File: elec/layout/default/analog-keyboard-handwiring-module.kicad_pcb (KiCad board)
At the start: 2 copper layers, 95.2 x 95.2 mm, 224 parts

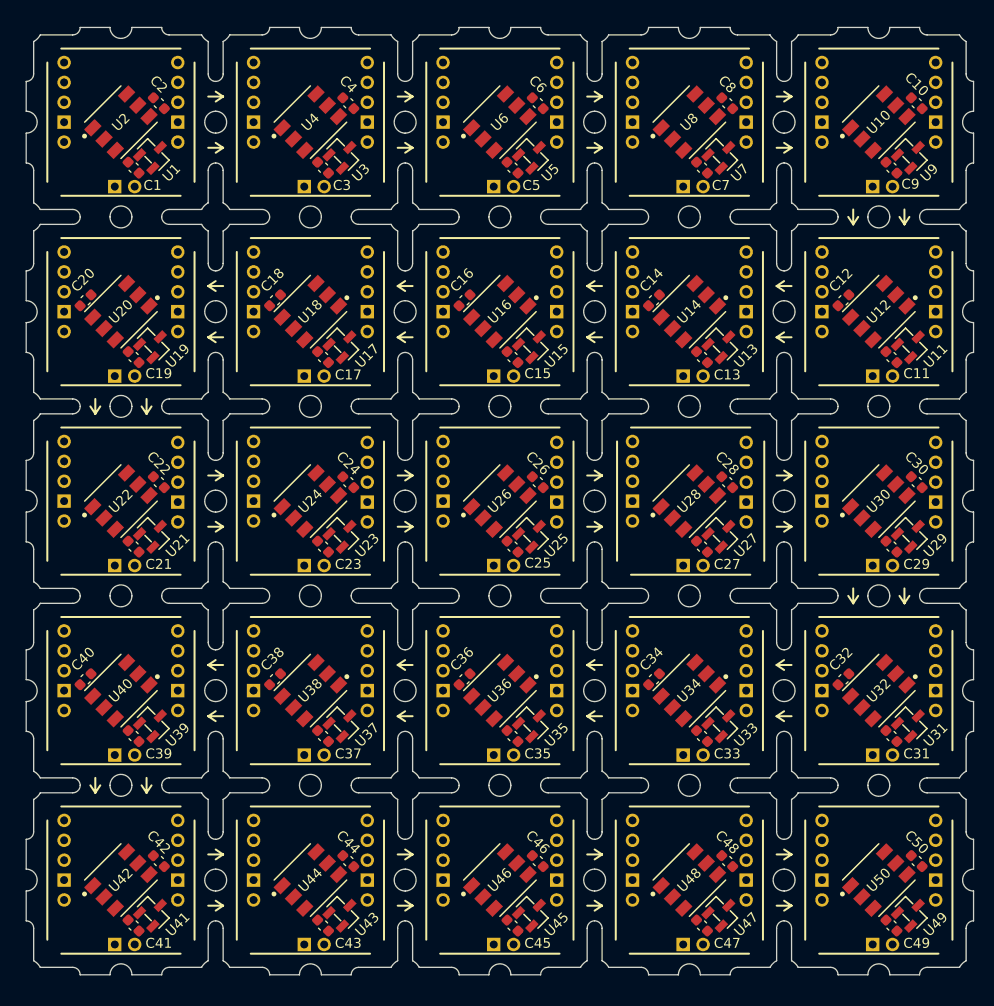
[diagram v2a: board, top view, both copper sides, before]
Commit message: Improve labels and move hall signal connector a little
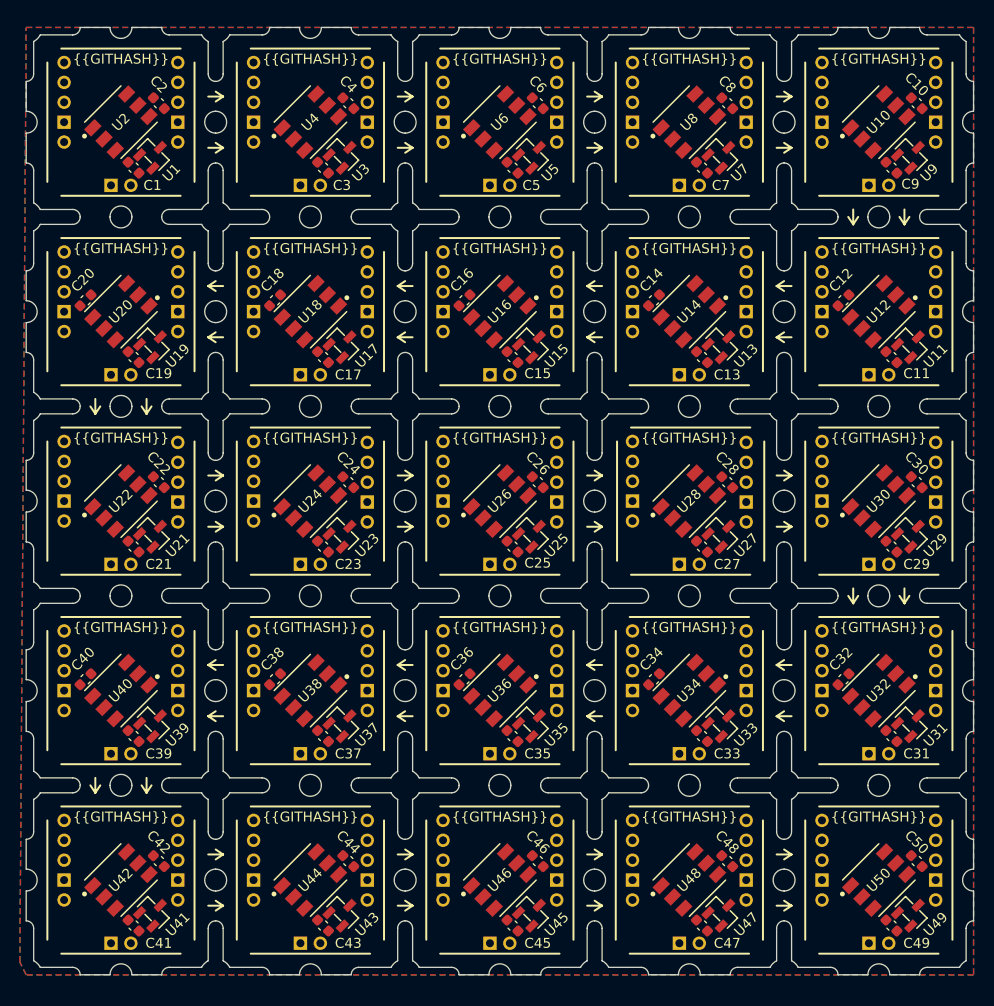
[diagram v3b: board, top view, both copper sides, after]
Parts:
- added kibuzzard-6658D545: G***, kibuzzard-6658D545, B.Cu at (56.3, 129.7)
- added kibuzzard-6658D545: G***, kibuzzard-6658D545, B.Cu at (113.5, 129.7)
- added kibuzzard-6658D545: G***, kibuzzard-6658D545, B.Cu at (113.5, 53.5)
- added kibuzzard-6658D545: G***, kibuzzard-6658D545, B.Cu at (113.5, 91.6)
- added kibuzzard-6658D545: G***, kibuzzard-6658D545, B.Cu at (132.5, 91.6)
- added kibuzzard-6658D545: G***, kibuzzard-6658D545, B.Cu at (75.4, 129.7)
- added kibuzzard-6658D545: G***, kibuzzard-6658D545, B.Cu at (94.4, 53.5)
- added kibuzzard-6658D545: G***, kibuzzard-6658D545, B.Cu at (94.4, 129.7)
- added kibuzzard-6658D545: G***, kibuzzard-6658D545, B.Cu at (56.3, 91.6)
- added kibuzzard-6658D545: G***, kibuzzard-6658D545, B.Cu at (94.4, 91.6)
- added kibuzzard-6658D545: G***, kibuzzard-6658D545, B.Cu at (75.4, 53.5)
- added kibuzzard-6658D545: G***, kibuzzard-6658D545, B.Cu at (56.3, 53.5)
- added kibuzzard-6658D545: G***, kibuzzard-6658D545, B.Cu at (132.5, 53.5)
- added kibuzzard-6658D545: G***, kibuzzard-6658D545, B.Cu at (75.4, 91.6)
- added kibuzzard-6658D545: G***, kibuzzard-6658D545, B.Cu at (132.5, 129.7)
- added kibuzzard-6658D54E: G***, kibuzzard-6658D54E, B.Cu at (75.4, 131.7)
- added kibuzzard-6658D54E: G***, kibuzzard-6658D54E, B.Cu at (56.3, 93.6)
- added kibuzzard-6658D54E: G***, kibuzzard-6658D54E, B.Cu at (113.5, 93.6)
- added kibuzzard-6658D54E: G***, kibuzzard-6658D54E, B.Cu at (56.3, 131.7)
- added kibuzzard-6658D54E: G***, kibuzzard-6658D54E, B.Cu at (94.4, 93.6)
- added kibuzzard-6658D54E: G***, kibuzzard-6658D54E, B.Cu at (132.5, 55.5)
- added kibuzzard-6658D54E: G***, kibuzzard-6658D54E, B.Cu at (94.4, 55.5)
- added kibuzzard-6658D54E: G***, kibuzzard-6658D54E, B.Cu at (113.5, 131.7)
- added kibuzzard-6658D54E: G***, kibuzzard-6658D54E, B.Cu at (56.3, 55.5)
- added kibuzzard-6658D54E: G***, kibuzzard-6658D54E, B.Cu at (75.4, 93.6)
- added kibuzzard-6658D54E: G***, kibuzzard-6658D54E, B.Cu at (132.5, 131.7)
- added kibuzzard-6658D54E: G***, kibuzzard-6658D54E, B.Cu at (113.5, 55.5)
- added kibuzzard-6658D54E: G***, kibuzzard-6658D54E, B.Cu at (132.5, 93.6)
- added kibuzzard-6658D54E: G***, kibuzzard-6658D54E, B.Cu at (94.4, 131.7)
- added kibuzzard-6658D54E: G***, kibuzzard-6658D54E, B.Cu at (75.4, 55.5)
- added kibuzzard-6658D556: G***, kibuzzard-6658D556, B.Cu at (56.8, 133.7)
- added kibuzzard-6658D556: G***, kibuzzard-6658D556, B.Cu at (94.9, 114.7)
- added kibuzzard-6658D556: G***, kibuzzard-6658D556, B.Cu at (56.8, 57.5)
- added kibuzzard-6658D556: G***, kibuzzard-6658D556, B.Cu at (94.9, 76.6)
- added kibuzzard-6658D556: G***, kibuzzard-6658D556, B.Cu at (75.8, 114.7)
- added kibuzzard-6658D556: G***, kibuzzard-6658D556, B.Cu at (133.0, 76.6)
- added kibuzzard-6658D556: G***, kibuzzard-6658D556, B.Cu at (75.8, 57.5)
- added kibuzzard-6658D556: G***, kibuzzard-6658D556, B.Cu at (133.0, 114.7)
- added kibuzzard-6658D556: G***, kibuzzard-6658D556, B.Cu at (133.0, 95.6)
- added kibuzzard-6658D556: G***, kibuzzard-6658D556, B.Cu at (94.9, 57.5)
- added kibuzzard-6658D556: G***, kibuzzard-6658D556, B.Cu at (75.8, 95.6)
- added kibuzzard-6658D556: G***, kibuzzard-6658D556, B.Cu at (56.8, 114.7)
- added kibuzzard-6658D556: G***, kibuzzard-6658D556, B.Cu at (94.9, 133.7)
- added kibuzzard-6658D556: G***, kibuzzard-6658D556, B.Cu at (113.9, 57.5)
- added kibuzzard-6658D556: G***, kibuzzard-6658D556, B.Cu at (113.9, 95.6)
- added kibuzzard-6658D556: G***, kibuzzard-6658D556, B.Cu at (133.0, 57.5)
- added kibuzzard-6658D556: G***, kibuzzard-6658D556, B.Cu at (113.9, 133.7)
- added kibuzzard-6658D556: G***, kibuzzard-6658D556, B.Cu at (56.8, 95.6)
- added kibuzzard-6658D556: G***, kibuzzard-6658D556, B.Cu at (113.9, 76.6)
- added kibuzzard-6658D556: G***, kibuzzard-6658D556, B.Cu at (56.8, 76.6)
- added kibuzzard-6658D556: G***, kibuzzard-6658D556, B.Cu at (75.8, 76.6)
- added kibuzzard-6658D556: G***, kibuzzard-6658D556, B.Cu at (133.0, 133.7)
- added kibuzzard-6658D556: G***, kibuzzard-6658D556, B.Cu at (94.9, 95.6)
- added kibuzzard-6658D556: G***, kibuzzard-6658D556, B.Cu at (113.9, 114.7)
- added kibuzzard-6658D556: G***, kibuzzard-6658D556, B.Cu at (75.8, 133.7)
- added kibuzzard-6658D562: G***, kibuzzard-6658D562, B.Cu at (94.5, 59.5)
- added kibuzzard-6658D562: G***, kibuzzard-6658D562, B.Cu at (94.5, 116.7)
- added kibuzzard-6658D562: G***, kibuzzard-6658D562, B.Cu at (56.4, 59.5)
- added kibuzzard-6658D562: G***, kibuzzard-6658D562, B.Cu at (75.4, 97.6)
- added kibuzzard-6658D562: G***, kibuzzard-6658D562, B.Cu at (75.4, 116.7)
- added kibuzzard-6658D562: G***, kibuzzard-6658D562, B.Cu at (94.5, 135.7)
- added kibuzzard-6658D562: G***, kibuzzard-6658D562, B.Cu at (132.6, 116.7)
- added kibuzzard-6658D562: G***, kibuzzard-6658D562, B.Cu at (94.5, 97.6)
- added kibuzzard-6658D562: G***, kibuzzard-6658D562, B.Cu at (56.4, 116.7)
- added kibuzzard-6658D562: G***, kibuzzard-6658D562, B.Cu at (75.4, 135.7)
- added kibuzzard-6658D562: G***, kibuzzard-6658D562, B.Cu at (113.5, 59.5)
- added kibuzzard-6658D562: G***, kibuzzard-6658D562, B.Cu at (75.4, 78.6)
- added kibuzzard-6658D562: G***, kibuzzard-6658D562, B.Cu at (113.5, 135.7)
- added kibuzzard-6658D562: G***, kibuzzard-6658D562, B.Cu at (113.5, 78.6)
- added kibuzzard-6658D562: G***, kibuzzard-6658D562, B.Cu at (94.5, 78.6)
- added kibuzzard-6658D562: G***, kibuzzard-6658D562, B.Cu at (56.4, 78.6)
- added kibuzzard-6658D562: G***, kibuzzard-6658D562, B.Cu at (113.5, 116.7)
- added kibuzzard-6658D562: G***, kibuzzard-6658D562, B.Cu at (75.4, 59.5)
- added kibuzzard-6658D562: G***, kibuzzard-6658D562, B.Cu at (56.4, 97.6)
- added kibuzzard-6658D562: G***, kibuzzard-6658D562, B.Cu at (132.6, 59.5)
- added kibuzzard-6658D562: G***, kibuzzard-6658D562, B.Cu at (132.6, 78.6)
- added kibuzzard-6658D562: G***, kibuzzard-6658D562, B.Cu at (56.4, 135.7)
- added kibuzzard-6658D562: G***, kibuzzard-6658D562, B.Cu at (132.6, 97.6)
- added kibuzzard-6658D562: G***, kibuzzard-6658D562, B.Cu at (132.6, 135.7)
- added kibuzzard-6658D562: G***, kibuzzard-6658D562, B.Cu at (113.5, 97.6)
- added kibuzzard-6658D56A: G***, kibuzzard-6658D56A, B.Cu at (94.9, 99.6)
- added kibuzzard-6658D56A: G***, kibuzzard-6658D56A, B.Cu at (75.8, 61.5)
- added kibuzzard-6658D56A: G***, kibuzzard-6658D56A, B.Cu at (94.9, 137.7)
- added kibuzzard-6658D56A: G***, kibuzzard-6658D56A, B.Cu at (94.9, 118.7)
- added kibuzzard-6658D56A: G***, kibuzzard-6658D56A, B.Cu at (113.9, 99.6)
- added kibuzzard-6658D56A: G***, kibuzzard-6658D56A, B.Cu at (113.9, 80.6)
- added kibuzzard-6658D56A: G***, kibuzzard-6658D56A, B.Cu at (56.8, 99.6)
- added kibuzzard-6658D56A: G***, kibuzzard-6658D56A, B.Cu at (75.8, 80.6)
- added kibuzzard-6658D56A: G***, kibuzzard-6658D56A, B.Cu at (133.0, 80.6)
- added kibuzzard-6658D56A: G***, kibuzzard-6658D56A, B.Cu at (113.9, 137.7)
- added kibuzzard-6658D56A: G***, kibuzzard-6658D56A, B.Cu at (56.8, 118.7)
- added kibuzzard-6658D56A: G***, kibuzzard-6658D56A, B.Cu at (75.8, 118.7)
- added kibuzzard-6658D56A: G***, kibuzzard-6658D56A, B.Cu at (94.9, 80.6)
- added kibuzzard-6658D56A: G***, kibuzzard-6658D56A, B.Cu at (113.9, 61.5)
- added kibuzzard-6658D56A: G***, kibuzzard-6658D56A, B.Cu at (75.8, 137.7)
- added kibuzzard-6658D56A: G***, kibuzzard-6658D56A, B.Cu at (56.8, 137.7)
- added kibuzzard-6658D56A: G***, kibuzzard-6658D56A, B.Cu at (133.0, 137.7)
- added kibuzzard-6658D56A: G***, kibuzzard-6658D56A, B.Cu at (75.8, 99.6)
- added kibuzzard-6658D56A: G***, kibuzzard-6658D56A, B.Cu at (94.9, 61.5)
- added kibuzzard-6658D56A: G***, kibuzzard-6658D56A, B.Cu at (133.0, 99.6)
- added kibuzzard-6658D56A: G***, kibuzzard-6658D56A, B.Cu at (133.0, 61.5)
- added kibuzzard-6658D56A: G***, kibuzzard-6658D56A, B.Cu at (56.8, 61.5)
- added kibuzzard-6658D56A: G***, kibuzzard-6658D56A, B.Cu at (113.9, 118.7)
- added kibuzzard-6658D56A: G***, kibuzzard-6658D56A, B.Cu at (56.8, 80.6)
- added kibuzzard-6658D56A: G***, kibuzzard-6658D56A, B.Cu at (133.0, 118.7)
- added kibuzzard-6658D6DF: G***, kibuzzard-6658D6DF, B.Cu at (114.9, 64.1)
- added kibuzzard-6658D6DF: G***, kibuzzard-6658D6DF, B.Cu at (57.7, 64.1)
- added kibuzzard-6658D6DF: G***, kibuzzard-6658D6DF, B.Cu at (57.7, 83.1)
- added kibuzzard-6658D6DF: G***, kibuzzard-6658D6DF, B.Cu at (114.9, 140.3)
- added kibuzzard-6658D6DF: G***, kibuzzard-6658D6DF, B.Cu at (133.9, 140.3)
- added kibuzzard-6658D6DF: G***, kibuzzard-6658D6DF, B.Cu at (57.7, 102.2)
- added kibuzzard-6658D6DF: G***, kibuzzard-6658D6DF, B.Cu at (114.9, 121.2)
- added kibuzzard-6658D6DF: G***, kibuzzard-6658D6DF, B.Cu at (76.8, 64.1)
- added kibuzzard-6658D6DF: G***, kibuzzard-6658D6DF, B.Cu at (76.8, 121.2)
- added kibuzzard-6658D6DF: G***, kibuzzard-6658D6DF, B.Cu at (95.8, 64.1)
- added kibuzzard-6658D6DF: G***, kibuzzard-6658D6DF, B.Cu at (114.9, 102.2)
- added kibuzzard-6658D6DF: G***, kibuzzard-6658D6DF, B.Cu at (95.8, 102.2)
- added kibuzzard-6658D6DF: G***, kibuzzard-6658D6DF, B.Cu at (133.9, 102.2)
- added kibuzzard-6658D6DF: G***, kibuzzard-6658D6DF, B.Cu at (95.8, 83.1)
- added kibuzzard-6658D6DF: G***, kibuzzard-6658D6DF, B.Cu at (76.8, 102.2)
- added kibuzzard-6658D6DF: G***, kibuzzard-6658D6DF, B.Cu at (133.9, 121.2)
- added kibuzzard-6658D6DF: G***, kibuzzard-6658D6DF, B.Cu at (76.8, 140.3)
- added kibuzzard-6658D6DF: G***, kibuzzard-6658D6DF, B.Cu at (57.7, 140.3)
- added kibuzzard-6658D6DF: G***, kibuzzard-6658D6DF, B.Cu at (133.9, 64.1)
- added kibuzzard-6658D6DF: G***, kibuzzard-6658D6DF, B.Cu at (95.8, 140.3)
- added kibuzzard-6658D6DF: G***, kibuzzard-6658D6DF, B.Cu at (114.9, 83.1)
- added kibuzzard-6658D6DF: G***, kibuzzard-6658D6DF, B.Cu at (133.9, 83.1)
- added kibuzzard-6658D6DF: G***, kibuzzard-6658D6DF, B.Cu at (76.8, 83.1)
- added kibuzzard-6658D6DF: G***, kibuzzard-6658D6DF, B.Cu at (57.7, 121.2)
- added kibuzzard-6658D6DF: G***, kibuzzard-6658D6DF, B.Cu at (95.8, 121.2)
- added kibuzzard-6658D76C: G***, kibuzzard-6658D76C, B.Cu at (75.0, 104.0)
- added kibuzzard-6658D76C: G***, kibuzzard-6658D76C, B.Cu at (56.0, 142.1)
- added kibuzzard-6658D76C: G***, kibuzzard-6658D76C, B.Cu at (113.1, 142.1)
- added kibuzzard-6658D76C: G***, kibuzzard-6658D76C, B.Cu at (94.1, 65.9)
- added kibuzzard-6658D76C: G***, kibuzzard-6658D76C, B.Cu at (56.0, 65.9)
- added kibuzzard-6658D76C: G***, kibuzzard-6658D76C, B.Cu at (94.1, 123.0)
- added kibuzzard-6658D76C: G***, kibuzzard-6658D76C, B.Cu at (56.0, 123.0)
- added kibuzzard-6658D76C: G***, kibuzzard-6658D76C, B.Cu at (132.2, 104.0)
- added kibuzzard-6658D76C: G***, kibuzzard-6658D76C, B.Cu at (132.2, 142.1)
- added kibuzzard-6658D76C: G***, kibuzzard-6658D76C, B.Cu at (56.0, 104.0)
- added kibuzzard-6658D76C: G***, kibuzzard-6658D76C, B.Cu at (75.0, 65.9)
- added kibuzzard-6658D76C: G***, kibuzzard-6658D76C, B.Cu at (75.0, 142.1)
- added kibuzzard-6658D76C: G***, kibuzzard-6658D76C, B.Cu at (113.1, 104.0)
- added kibuzzard-6658D76C: G***, kibuzzard-6658D76C, B.Cu at (113.1, 123.0)
- added kibuzzard-6658D76C: G***, kibuzzard-6658D76C, B.Cu at (132.2, 84.9)
- added kibuzzard-6658D76C: G***, kibuzzard-6658D76C, B.Cu at (113.1, 65.9)
- added kibuzzard-6658D76C: G***, kibuzzard-6658D76C, B.Cu at (113.1, 84.9)
- added kibuzzard-6658D76C: G***, kibuzzard-6658D76C, B.Cu at (94.1, 84.9)
- added kibuzzard-6658D76C: G***, kibuzzard-6658D76C, B.Cu at (56.0, 84.9)
- added kibuzzard-6658D76C: G***, kibuzzard-6658D76C, B.Cu at (132.2, 65.9)
- added kibuzzard-6658D76C: G***, kibuzzard-6658D76C, B.Cu at (75.0, 84.9)
- added kibuzzard-6658D76C: G***, kibuzzard-6658D76C, B.Cu at (94.1, 104.0)
- added kibuzzard-6658D76C: G***, kibuzzard-6658D76C, B.Cu at (75.0, 123.0)
- added kibuzzard-6658D76C: G***, kibuzzard-6658D76C, B.Cu at (94.1, 142.1)
- added kibuzzard-6658D76C: G***, kibuzzard-6658D76C, B.Cu at (132.2, 123.0)
- added kibuzzard-6658D7A0: G***, kibuzzard-6658D7A0, B.Cu at (100.8, 91.6)
- added kibuzzard-6658D7A0: G***, kibuzzard-6658D7A0, B.Cu at (119.9, 129.7)
- added kibuzzard-6658D7A0: G***, kibuzzard-6658D7A0, B.Cu at (138.9, 91.6)
- added kibuzzard-6658D7A0: G***, kibuzzard-6658D7A0, B.Cu at (100.8, 129.7)
- added kibuzzard-6658D7A0: G***, kibuzzard-6658D7A0, B.Cu at (138.9, 53.5)
- added kibuzzard-6658D7A0: G***, kibuzzard-6658D7A0, B.Cu at (119.9, 53.5)
- added kibuzzard-6658D7A0: G***, kibuzzard-6658D7A0, B.Cu at (138.9, 129.7)
- added kibuzzard-6658D7A0: G***, kibuzzard-6658D7A0, B.Cu at (81.8, 129.7)
- added kibuzzard-6658D7A0: G***, kibuzzard-6658D7A0, B.Cu at (81.8, 91.6)
- added kibuzzard-6658D7A0: G***, kibuzzard-6658D7A0, B.Cu at (62.7, 129.7)
- added kibuzzard-6658D7A0: G***, kibuzzard-6658D7A0, B.Cu at (100.8, 53.5)
- added kibuzzard-6658D7A0: G***, kibuzzard-6658D7A0, B.Cu at (119.9, 91.6)
- added kibuzzard-6658D7A0: G***, kibuzzard-6658D7A0, B.Cu at (62.7, 91.6)
- added kibuzzard-6658D7A0: G***, kibuzzard-6658D7A0, B.Cu at (81.8, 53.5)
- added kibuzzard-6658D7A0: G***, kibuzzard-6658D7A0, B.Cu at (62.7, 53.5)
- added kibuzzard-6658D7B3: G***, kibuzzard-6658D7B3, B.Cu at (100.8, 93.6)
- added kibuzzard-6658D7B3: G***, kibuzzard-6658D7B3, B.Cu at (119.8, 93.6)
- added kibuzzard-6658D7B3: G***, kibuzzard-6658D7B3, B.Cu at (138.9, 131.7)
- added kibuzzard-6658D7B3: G***, kibuzzard-6658D7B3, B.Cu at (119.8, 55.5)
- added kibuzzard-6658D7B3: G***, kibuzzard-6658D7B3, B.Cu at (100.8, 131.7)
- added kibuzzard-6658D7B3: G***, kibuzzard-6658D7B3, B.Cu at (119.8, 131.7)
- added kibuzzard-6658D7B3: G***, kibuzzard-6658D7B3, B.Cu at (100.8, 55.5)
- added kibuzzard-6658D7B3: G***, kibuzzard-6658D7B3, B.Cu at (138.9, 93.6)
- added kibuzzard-6658D7B3: G***, kibuzzard-6658D7B3, B.Cu at (81.8, 93.6)
- added kibuzzard-6658D7B3: G***, kibuzzard-6658D7B3, B.Cu at (81.8, 55.5)
- added kibuzzard-6658D7B3: G***, kibuzzard-6658D7B3, B.Cu at (81.8, 131.7)
- added kibuzzard-6658D7B3: G***, kibuzzard-6658D7B3, B.Cu at (138.9, 55.5)
- added kibuzzard-6658D7B3: G***, kibuzzard-6658D7B3, B.Cu at (62.7, 131.7)
- added kibuzzard-6658D7B3: G***, kibuzzard-6658D7B3, B.Cu at (62.7, 93.6)
- added kibuzzard-6658D7B3: G***, kibuzzard-6658D7B3, B.Cu at (62.7, 55.5)
- added kibuzzard-6658D7BA: G***, kibuzzard-6658D7BA, B.Cu at (100.4, 95.6)
- added kibuzzard-6658D7BA: G***, kibuzzard-6658D7BA, B.Cu at (119.4, 114.7)
- added kibuzzard-6658D7BA: G***, kibuzzard-6658D7BA, B.Cu at (100.4, 133.7)
- added kibuzzard-6658D7BA: G***, kibuzzard-6658D7BA, B.Cu at (81.3, 133.7)
- added kibuzzard-6658D7BA: G***, kibuzzard-6658D7BA, B.Cu at (138.5, 133.7)
- added kibuzzard-6658D7BA: G***, kibuzzard-6658D7BA, B.Cu at (62.3, 95.6)
- added kibuzzard-6658D7BA: G***, kibuzzard-6658D7BA, B.Cu at (138.5, 95.6)
- added kibuzzard-6658D7BA: G***, kibuzzard-6658D7BA, B.Cu at (81.3, 57.5)
- added kibuzzard-6658D7BA: G***, kibuzzard-6658D7BA, B.Cu at (81.3, 76.6)
- added kibuzzard-6658D7BA: G***, kibuzzard-6658D7BA, B.Cu at (62.3, 57.5)
- added kibuzzard-6658D7BA: G***, kibuzzard-6658D7BA, B.Cu at (100.4, 76.6)
- added kibuzzard-6658D7BA: G***, kibuzzard-6658D7BA, B.Cu at (81.3, 95.6)
- added kibuzzard-6658D7BA: G***, kibuzzard-6658D7BA, B.Cu at (100.4, 114.7)
- added kibuzzard-6658D7BA: G***, kibuzzard-6658D7BA, B.Cu at (119.4, 76.6)
- added kibuzzard-6658D7BA: G***, kibuzzard-6658D7BA, B.Cu at (62.3, 76.6)
- added kibuzzard-6658D7BA: G***, kibuzzard-6658D7BA, B.Cu at (62.3, 133.7)
- added kibuzzard-6658D7BA: G***, kibuzzard-6658D7BA, B.Cu at (119.4, 57.5)
- added kibuzzard-6658D7BA: G***, kibuzzard-6658D7BA, B.Cu at (138.5, 114.7)
- added kibuzzard-6658D7BA: G***, kibuzzard-6658D7BA, B.Cu at (81.3, 114.7)
- added kibuzzard-6658D7BA: G***, kibuzzard-6658D7BA, B.Cu at (138.5, 76.6)
- added kibuzzard-6658D7BA: G***, kibuzzard-6658D7BA, B.Cu at (62.3, 114.7)
- added kibuzzard-6658D7BA: G***, kibuzzard-6658D7BA, B.Cu at (138.5, 57.5)
- added kibuzzard-6658D7BA: G***, kibuzzard-6658D7BA, B.Cu at (119.4, 133.7)
- added kibuzzard-6658D7BA: G***, kibuzzard-6658D7BA, B.Cu at (119.4, 95.6)
- added kibuzzard-6658D7BA: G***, kibuzzard-6658D7BA, B.Cu at (100.4, 57.5)
- added kibuzzard-6658D7C3: G***, kibuzzard-6658D7C3, B.Cu at (62.7, 135.7)
- added kibuzzard-6658D7C3: G***, kibuzzard-6658D7C3, B.Cu at (119.8, 135.7)
- added kibuzzard-6658D7C3: G***, kibuzzard-6658D7C3, B.Cu at (62.7, 59.5)
- added kibuzzard-6658D7C3: G***, kibuzzard-6658D7C3, B.Cu at (81.8, 59.5)
- added kibuzzard-6658D7C3: G***, kibuzzard-6658D7C3, B.Cu at (62.7, 97.6)
- added kibuzzard-6658D7C3: G***, kibuzzard-6658D7C3, B.Cu at (62.7, 78.6)
- added kibuzzard-6658D7C3: G***, kibuzzard-6658D7C3, B.Cu at (138.9, 59.5)
- added kibuzzard-6658D7C3: G***, kibuzzard-6658D7C3, B.Cu at (100.8, 78.6)
- added kibuzzard-6658D7C3: G***, kibuzzard-6658D7C3, B.Cu at (100.8, 97.6)
- added kibuzzard-6658D7C3: G***, kibuzzard-6658D7C3, B.Cu at (62.7, 116.7)
- added kibuzzard-6658D7C3: G***, kibuzzard-6658D7C3, B.Cu at (119.8, 97.6)
- added kibuzzard-6658D7C3: G***, kibuzzard-6658D7C3, B.Cu at (138.9, 97.6)
- added kibuzzard-6658D7C3: G***, kibuzzard-6658D7C3, B.Cu at (81.8, 97.6)
- added kibuzzard-6658D7C3: G***, kibuzzard-6658D7C3, B.Cu at (138.9, 78.6)
- added kibuzzard-6658D7C3: G***, kibuzzard-6658D7C3, B.Cu at (100.8, 135.7)
- added kibuzzard-6658D7C3: G***, kibuzzard-6658D7C3, B.Cu at (81.8, 78.6)
- added kibuzzard-6658D7C3: G***, kibuzzard-6658D7C3, B.Cu at (81.8, 116.7)
- added kibuzzard-6658D7C3: G***, kibuzzard-6658D7C3, B.Cu at (81.8, 135.7)
- added kibuzzard-6658D7C3: G***, kibuzzard-6658D7C3, B.Cu at (119.8, 59.5)
- added kibuzzard-6658D7C3: G***, kibuzzard-6658D7C3, B.Cu at (119.8, 116.7)
- added kibuzzard-6658D7C3: G***, kibuzzard-6658D7C3, B.Cu at (100.8, 116.7)
- added kibuzzard-6658D7C3: G***, kibuzzard-6658D7C3, B.Cu at (119.8, 78.6)
- added kibuzzard-6658D7C3: G***, kibuzzard-6658D7C3, B.Cu at (138.9, 135.7)
- added kibuzzard-6658D7C3: G***, kibuzzard-6658D7C3, B.Cu at (138.9, 116.7)
- added kibuzzard-6658D7C3: G***, kibuzzard-6658D7C3, B.Cu at (100.8, 59.5)
- added kibuzzard-6658D7D5: G***, kibuzzard-6658D7D5, B.Cu at (138.5, 99.6)
- added kibuzzard-6658D7D5: G***, kibuzzard-6658D7D5, B.Cu at (138.5, 137.7)
- added kibuzzard-6658D7D5: G***, kibuzzard-6658D7D5, B.Cu at (62.3, 61.5)
- added kibuzzard-6658D7D5: G***, kibuzzard-6658D7D5, B.Cu at (81.3, 61.5)
- added kibuzzard-6658D7D5: G***, kibuzzard-6658D7D5, B.Cu at (100.4, 80.6)
- added kibuzzard-6658D7D5: G***, kibuzzard-6658D7D5, B.Cu at (81.3, 80.6)
- added kibuzzard-6658D7D5: G***, kibuzzard-6658D7D5, B.Cu at (62.3, 118.7)
- added kibuzzard-6658D7D5: G***, kibuzzard-6658D7D5, B.Cu at (119.4, 99.6)
- added kibuzzard-6658D7D5: G***, kibuzzard-6658D7D5, B.Cu at (62.3, 137.7)
- added kibuzzard-6658D7D5: G***, kibuzzard-6658D7D5, B.Cu at (100.4, 99.6)
- added kibuzzard-6658D7D5: G***, kibuzzard-6658D7D5, B.Cu at (119.4, 80.6)
- added kibuzzard-6658D7D5: G***, kibuzzard-6658D7D5, B.Cu at (81.3, 118.7)
- added kibuzzard-6658D7D5: G***, kibuzzard-6658D7D5, B.Cu at (119.4, 137.7)
- added kibuzzard-6658D7D5: G***, kibuzzard-6658D7D5, B.Cu at (62.3, 99.6)
- added kibuzzard-6658D7D5: G***, kibuzzard-6658D7D5, B.Cu at (81.3, 99.6)
- added kibuzzard-6658D7D5: G***, kibuzzard-6658D7D5, B.Cu at (119.4, 118.7)
- added kibuzzard-6658D7D5: G***, kibuzzard-6658D7D5, B.Cu at (100.4, 118.7)
- added kibuzzard-6658D7D5: G***, kibuzzard-6658D7D5, B.Cu at (138.5, 61.5)
- added kibuzzard-6658D7D5: G***, kibuzzard-6658D7D5, B.Cu at (62.3, 80.6)
- added kibuzzard-6658D7D5: G***, kibuzzard-6658D7D5, B.Cu at (81.3, 137.7)
- added kibuzzard-6658D7D5: G***, kibuzzard-6658D7D5, B.Cu at (100.4, 137.7)
- added kibuzzard-6658D7D5: G***, kibuzzard-6658D7D5, B.Cu at (138.5, 80.6)
- added kibuzzard-6658D7D5: G***, kibuzzard-6658D7D5, B.Cu at (100.4, 61.5)
- added kibuzzard-6658D7D5: G***, kibuzzard-6658D7D5, B.Cu at (138.5, 118.7)
- added kibuzzard-6658D7D5: G***, kibuzzard-6658D7D5, B.Cu at (119.4, 61.5)
- added kibuzzard-6658DB35: G***, kibuzzard-6658DB35, B.Cu at (100.8, 72.6)
- added kibuzzard-6658DB35: G***, kibuzzard-6658DB35, B.Cu at (81.8, 72.6)
- added kibuzzard-6658DB35: G***, kibuzzard-6658DB35, B.Cu at (62.7, 72.6)
- added kibuzzard-6658DB35: G***, kibuzzard-6658DB35, B.Cu at (119.9, 110.7)
- added kibuzzard-6658DB35: G***, kibuzzard-6658DB35, B.Cu at (138.9, 110.7)
- added kibuzzard-6658DB35: G***, kibuzzard-6658DB35, B.Cu at (100.8, 110.7)
- added kibuzzard-6658DB35: G***, kibuzzard-6658DB35, B.Cu at (138.9, 72.6)
- added kibuzzard-6658DB35: G***, kibuzzard-6658DB35, B.Cu at (62.7, 110.7)
- added kibuzzard-6658DB35: G***, kibuzzard-6658DB35, B.Cu at (81.8, 110.7)
- added kibuzzard-6658DB35: G***, kibuzzard-6658DB35, B.Cu at (119.9, 72.6)
- added kibuzzard-6658DB3E: G***, kibuzzard-6658DB3E, B.Cu at (62.7, 112.7)
- added kibuzzard-6658DB3E: G***, kibuzzard-6658DB3E, B.Cu at (81.8, 112.7)
- added kibuzzard-6658DB3E: G***, kibuzzard-6658DB3E, B.Cu at (62.7, 74.6)
- added kibuzzard-6658DB3E: G***, kibuzzard-6658DB3E, B.Cu at (119.8, 112.7)
- added kibuzzard-6658DB3E: G***, kibuzzard-6658DB3E, B.Cu at (138.9, 112.7)
- added kibuzzard-6658DB3E: G***, kibuzzard-6658DB3E, B.Cu at (100.8, 112.7)
- added kibuzzard-6658DB3E: G***, kibuzzard-6658DB3E, B.Cu at (138.9, 74.6)
- added kibuzzard-6658DB3E: G***, kibuzzard-6658DB3E, B.Cu at (81.8, 74.6)
- added kibuzzard-6658DB3E: G***, kibuzzard-6658DB3E, B.Cu at (119.8, 74.6)
- added kibuzzard-6658DB3E: G***, kibuzzard-6658DB3E, B.Cu at (100.8, 74.6)
- added kibuzzard-6658DB47: G***, kibuzzard-6658DB47, B.Cu at (75.4, 72.6)
- added kibuzzard-6658DB47: G***, kibuzzard-6658DB47, B.Cu at (132.5, 110.7)
- added kibuzzard-6658DB47: G***, kibuzzard-6658DB47, B.Cu at (56.3, 110.7)
- added kibuzzard-6658DB47: G***, kibuzzard-6658DB47, B.Cu at (113.5, 110.7)
- added kibuzzard-6658DB47: G***, kibuzzard-6658DB47, B.Cu at (94.4, 110.7)
- added kibuzzard-6658DB47: G***, kibuzzard-6658DB47, B.Cu at (75.4, 110.7)
- added kibuzzard-6658DB47: G***, kibuzzard-6658DB47, B.Cu at (56.3, 72.6)
- added kibuzzard-6658DB47: G***, kibuzzard-6658DB47, B.Cu at (113.5, 72.6)
- added kibuzzard-6658DB47: G***, kibuzzard-6658DB47, B.Cu at (94.4, 72.6)
- added kibuzzard-6658DB47: G***, kibuzzard-6658DB47, B.Cu at (132.5, 72.6)
- added kibuzzard-6658DB4D: G***, kibuzzard-6658DB4D, B.Cu at (75.4, 74.6)
- added kibuzzard-6658DB4D: G***, kibuzzard-6658DB4D, B.Cu at (132.5, 112.7)
- added kibuzzard-6658DB4D: G***, kibuzzard-6658DB4D, B.Cu at (94.4, 74.6)
- added kibuzzard-6658DB4D: G***, kibuzzard-6658DB4D, B.Cu at (113.5, 112.7)
- added kibuzzard-6658DB4D: G***, kibuzzard-6658DB4D, B.Cu at (113.5, 74.6)
- added kibuzzard-6658DB4D: G***, kibuzzard-6658DB4D, B.Cu at (56.3, 112.7)
- added kibuzzard-6658DB4D: G***, kibuzzard-6658DB4D, B.Cu at (94.4, 112.7)
- added kibuzzard-6658DB4D: G***, kibuzzard-6658DB4D, B.Cu at (132.5, 74.6)
- added kibuzzard-6658DB4D: G***, kibuzzard-6658DB4D, B.Cu at (56.3, 74.6)
- added kibuzzard-6658DB4D: G***, kibuzzard-6658DB4D, B.Cu at (75.4, 112.7)
- moved J18 0.40 mm to (134.7, 84.9)
- moved J21 0.40 mm to (115.7, 84.9)
- moved J24 0.40 mm to (96.6, 84.9)
- moved J27 0.40 mm to (77.6, 84.9)
- moved J30 0.40 mm to (58.5, 84.9)
- moved J33 0.40 mm to (58.5, 104.0)
- moved J36 0.40 mm to (77.6, 104.0)
- moved J39 0.40 mm to (96.6, 104.0)
- moved J42 0.40 mm to (115.7, 104.0)
- moved J45 0.40 mm to (134.7, 104.0)
- moved J63 0.40 mm to (58.5, 142.1)
- moved J66 0.40 mm to (77.6, 142.1)
- moved J69 0.40 mm to (96.6, 142.1)
- moved J72 0.40 mm to (115.7, 142.1)
- moved J75 0.40 mm to (134.7, 142.1)
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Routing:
- added copper zone on B.Cu, net gnd
- added copper zone on F.Cu, net gnd
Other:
- board text added: "{{GITHASH}}"
- board text removed: "CKI"
- board text removed: "CKO"
- board text removed: "GND"
- board text removed: "SDI"
- board text removed: "SDO"
- board text removed: "VCCH"
- board text removed: "VCCL"
- board text removed: "VLED"
